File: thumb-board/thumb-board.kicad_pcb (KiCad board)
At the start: 2 copper layers, 53 x 53 mm, 26 parts, among them IC1 TMAG5253BA1IQDMRR, IC10 TMAG5253BA1IQDMRR, IC11 TMAG5253BA1IQDMRR, IC12 TMAG5253BA1IQDMRR, IC2 TMAG5253BA1IQDMRR, IC3 TMAG5253BA1IQDMRR, IC4 TMAG5253BA1IQDMRR, IC5 TMAG5253BA1IQDMRR, IC6 TMAG5253BA1IQDMRR, IC7 TMAG5253BA1IQDMRR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

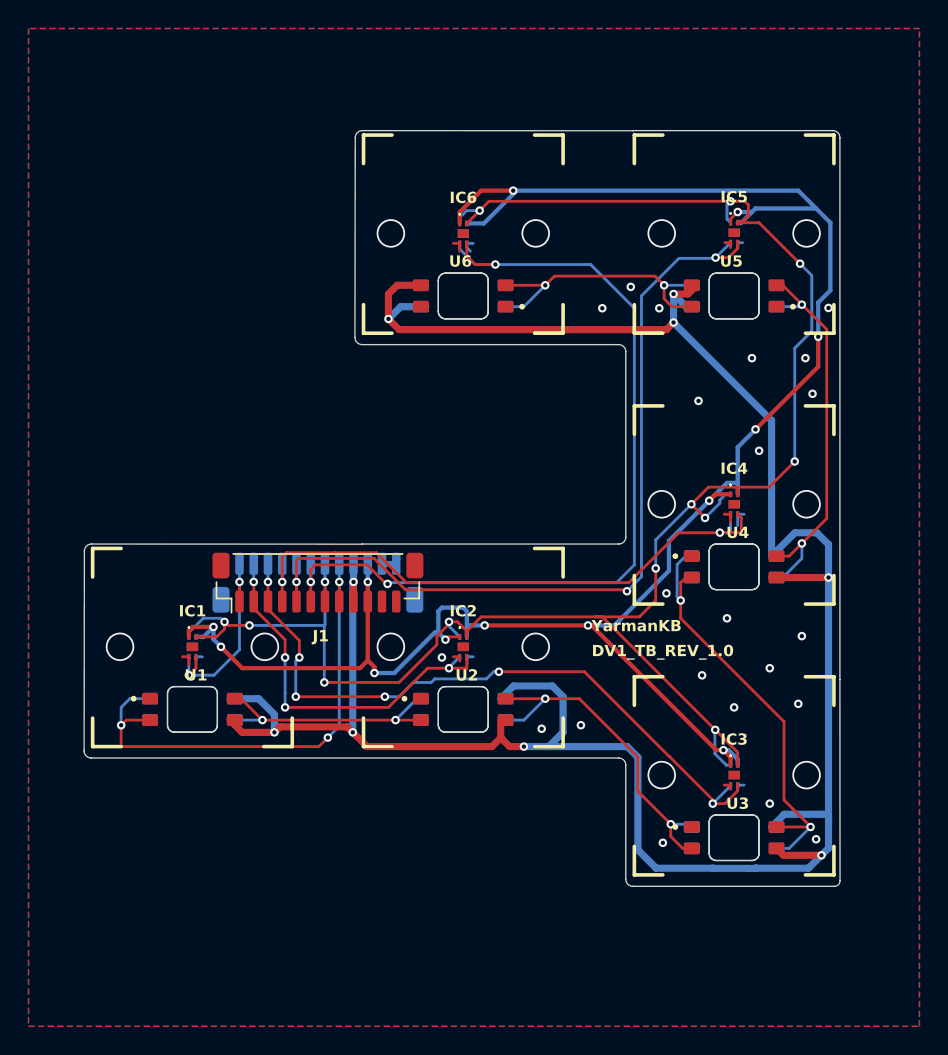
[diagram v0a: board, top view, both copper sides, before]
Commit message: Move SK6812 a bit down on daughter boards
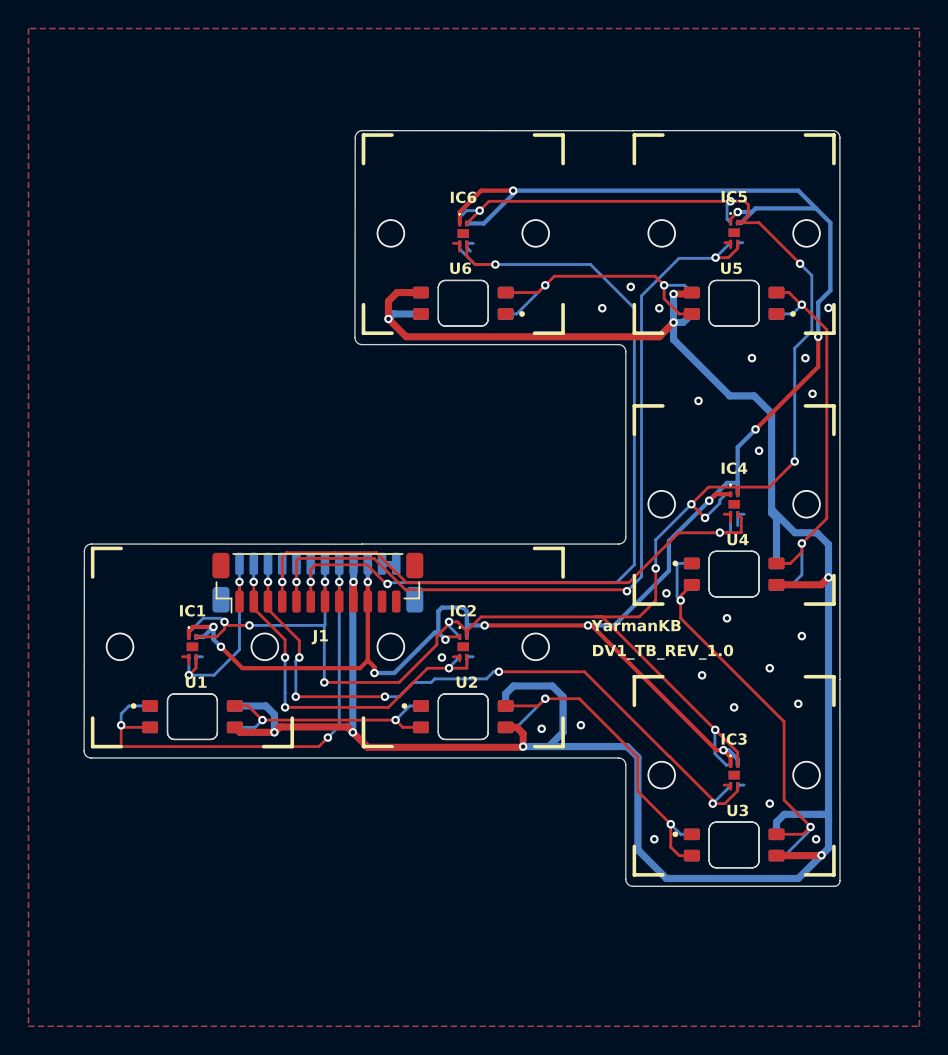
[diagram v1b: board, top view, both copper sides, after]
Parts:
- moved U1 0.51 mm to (116.5, 112.9)
- moved U10 0.51 mm to (154.5, 102.9)
- moved U11 0.51 mm to (154.5, 83.9)
- moved U12 0.51 mm to (135.5, 83.9)
- moved U2 0.51 mm to (135.5, 112.9)
- moved U3 0.51 mm to (154.5, 121.9)
- moved U4 0.51 mm to (154.5, 102.9)
- moved U5 0.51 mm to (154.5, 83.9)
- moved U6 0.51 mm to (135.5, 83.9)
- moved U7 0.51 mm to (116.5, 112.9)
- moved U8 0.51 mm to (135.5, 112.9)
- moved U9 0.51 mm to (154.5, 121.9)
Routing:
- net /D_2: track 32.5 -> 30.7 mm
- net /D_0: track 19.4 -> 18.0 mm
- net /DIN: track 36.6 -> 35.3 mm
- net /D_4: track 21.5 -> 20.9 mm

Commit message: Rename the board to Skadi
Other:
- board text added: "SKADI_TB_REV_1.0"
- board text removed: "DV1_TB_REV_1.0"
